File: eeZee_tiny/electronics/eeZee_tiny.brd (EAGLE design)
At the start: 21.8 x 17.8 mm, 8 parts, among them IC1 attiny, J2 avrisp

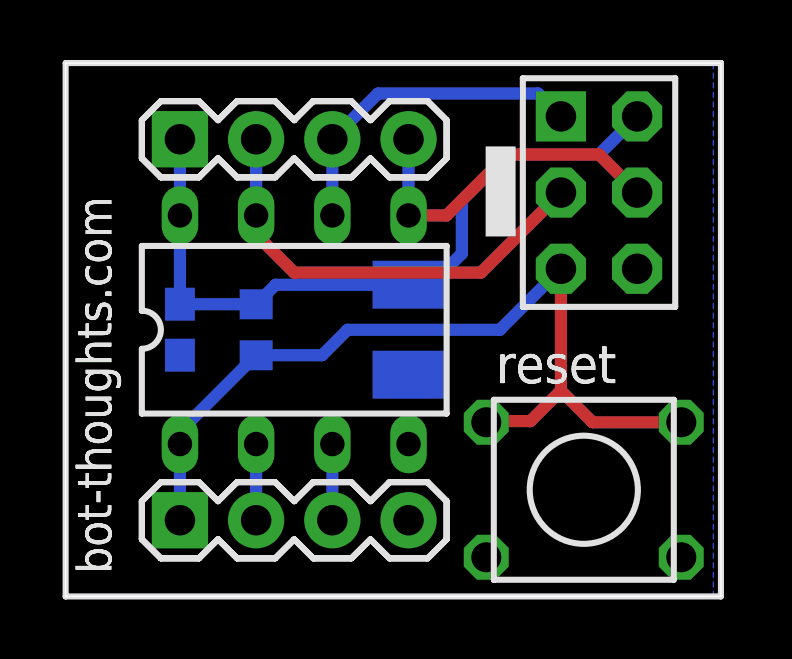
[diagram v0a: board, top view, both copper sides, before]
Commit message: Moved caps, mods to routing, added logos, added SCK indicator mark
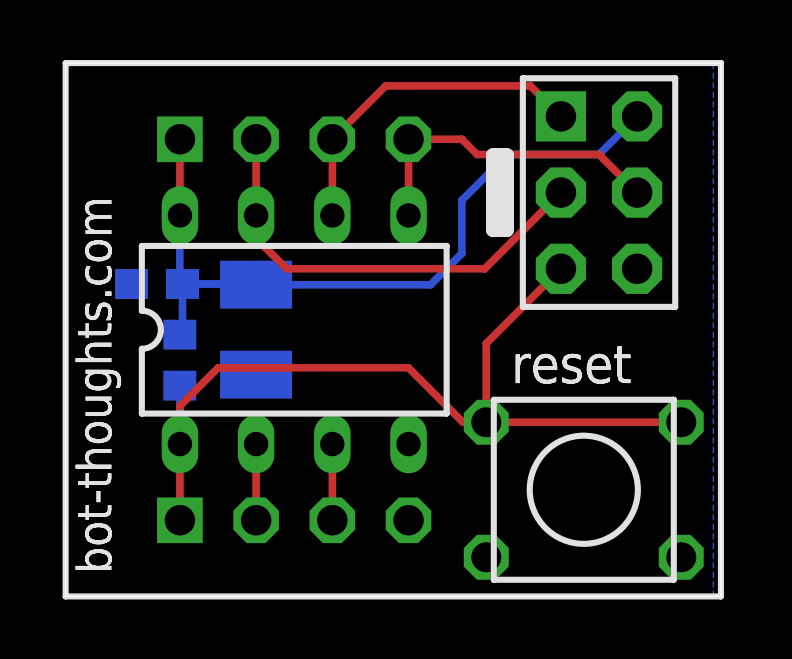
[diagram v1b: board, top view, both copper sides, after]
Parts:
- removed JP1, JP2: (no value), SparkFun:1X04
- added JP3, JP4: (no value), pinhead-2:1X04-S
- moved C2 5.08 mm to (6.35, 8.89)
- moved R1 2.74 mm to (3.81, 7.87)
- moved C1 1.70 mm to (3.05, 10.4), turned to 0 degrees
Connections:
- net !RESET: now also JP3.1; no longer JP1.1
- net GND: now also JP3.4; no longer JP1.4
- net MISO: now also JP4.3; no longer JP2.3
- net MOSI: now also JP4.4; no longer JP2.4
- net N$2: now also JP3.2; no longer JP1.2
- net N$8: now also JP3.3; no longer JP1.3
- net SCK: now also JP4.2; no longer JP2.2
- net VCC: now also JP4.1; no longer JP2.1
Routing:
- net VCC: track 24.4 -> 25.1 mm
- net MOSI: track 11.5 -> 10.9 mm
- net !RESET: track 29.3 -> 29.9 mm
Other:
- board text added: "Rev 0.2"

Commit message: Revised layout to reduce leading edge and side edge clearances for better breadboarding.
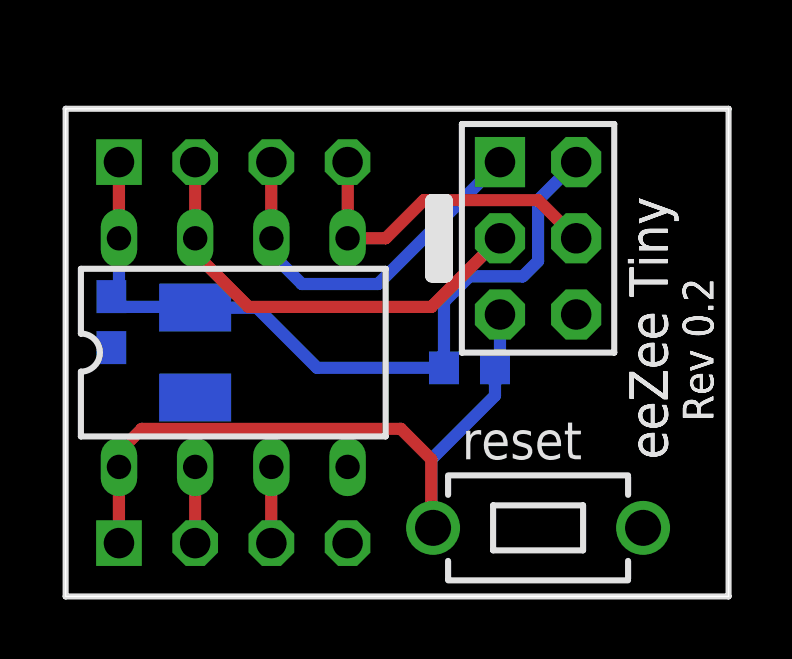
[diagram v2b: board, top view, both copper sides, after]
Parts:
- removed S2: reset, mes_electromech:6MMTACTILE_4PIN
- added S1: reset, mes_electromech:6MMTACTILE_RECT
- moved R1 9.66 mm to (13.5, 7.62), turned to 0 degrees
- moved J2 2.54 mm to (15.7, 11.9)
- moved C2 2.17 mm to (4.32, 8.13)
- moved IC1 2.17 mm to (5.59, 8.13)
- moved JP4 2.17 mm to (5.59, 14.5)
- moved JP3 2.17 mm to (5.59, 1.78)
- moved C1 1.98 mm to (1.52, 9.14), turned to 270 degrees
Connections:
- net !RESET: now also S1.P$1; no longer S2.B1, S2.B2
- net GND: now also S1.P$2; no longer S2.A1, S2.A2
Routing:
- net !RESET: track 29.9 -> 24.6 mm
- net VCC: track 25.1 -> 27.1 mm
- net MISO: track 11.3 -> 12.8 mm
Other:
- board size 21.8 x 17.8 mm -> 22.1 x 16.3 mm
- board text added: "eeZee Tiny"

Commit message: Revised board layout removing leading edge, using 6x3mm switch and making board narrower. Revised 8-pin tiny pad thickness minimum. Moved reset resistor for easier assembly. Revised and relocated logos.
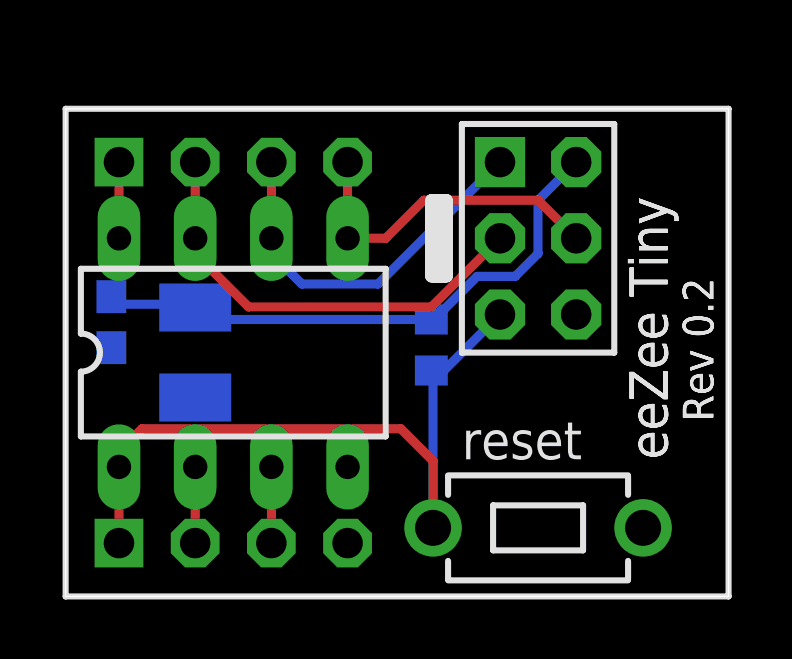
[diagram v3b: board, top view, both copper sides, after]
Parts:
- moved R1 1.48 mm to (12.2, 8.38), turned to 90 degrees
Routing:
- net VCC: track 27.1 -> 23.8 mm

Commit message: Rev 0.2, shrunk board, mitered corners, added polarity silk to tantalum.
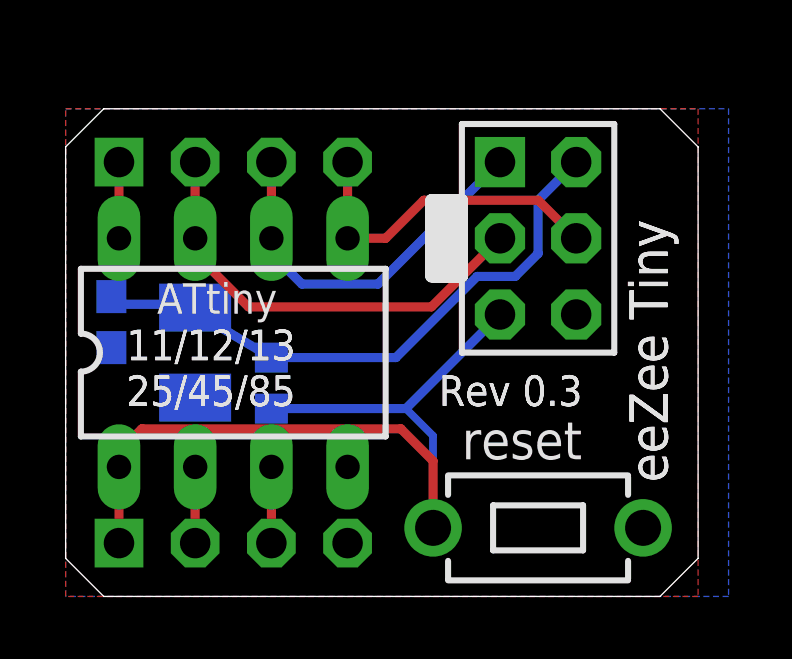
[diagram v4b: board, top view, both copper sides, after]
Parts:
- C2: device rcl:SMC_B -> mes_rcl:SMC_B
- IC1: value attiny -> ATtiny
- moved R1 5.48 mm to (6.86, 7.11)
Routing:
- net !RESET: track 24.8 -> 29.8 mm
- net VCC: track 23.8 -> 24.6 mm
- added copper zone on layer 1, net GND
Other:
- board size 22.1 x 16.3 mm -> 21.1 x 16.3 mm
- board text added: "11/12/13"
- board text added: "25/45/85"
- board text added: "ATtiny"
- board text added: "Rev 0.3"
- board text removed: "C1"
- board text removed: "C2"
- board text removed: "R1"
- board text removed: "Rev 0.2"
